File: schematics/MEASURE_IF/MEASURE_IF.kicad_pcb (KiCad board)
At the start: 2 copper layers, 45.7 x 65.2 mm, 50 parts, among them J1 SWD_CONN, J2 ARGUS_SPI_LEGACY_CONN, J3 ARGUS_SPI_FFC_CONN, J4 VMOT_IN_5mm, J5 MOT_TERM, J6 MOT_TERM, J7 USB_B_Micro, J8 MOT_TERM, J9 MOT_TERM, SW1 SW_RESET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

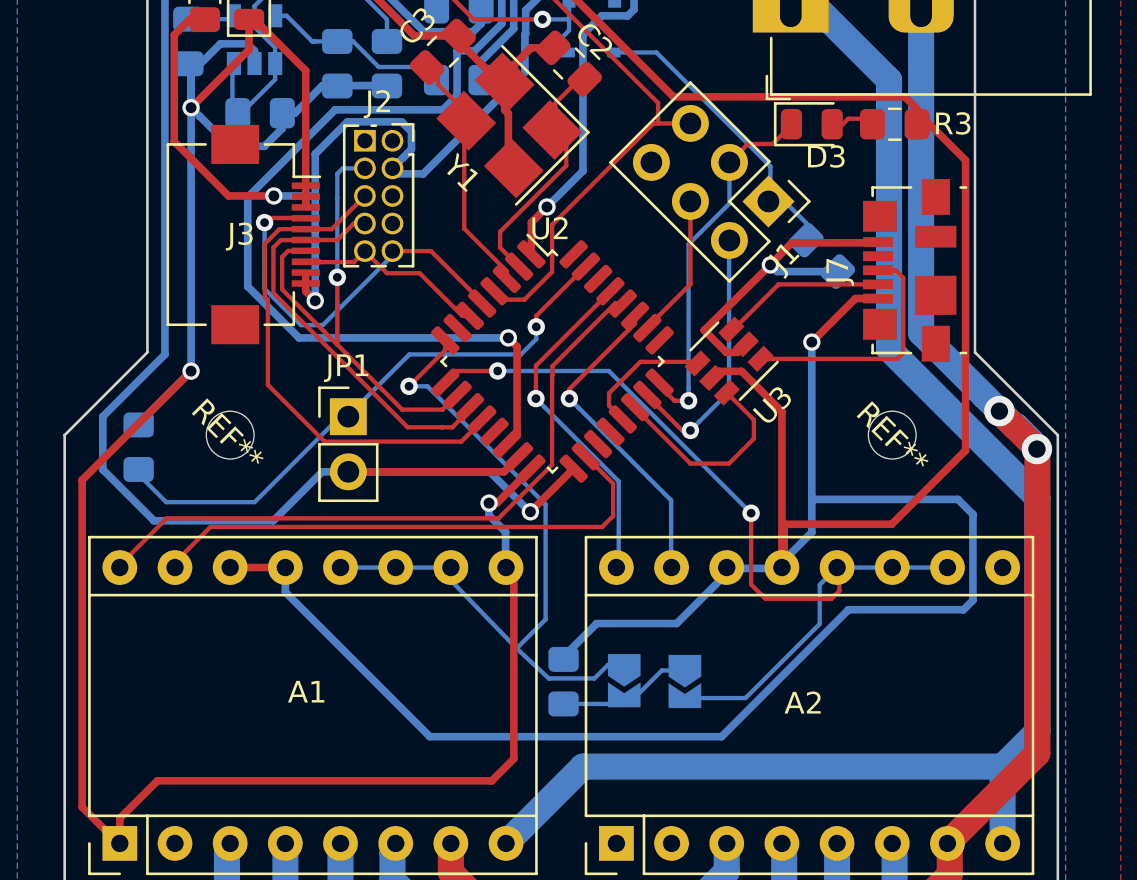
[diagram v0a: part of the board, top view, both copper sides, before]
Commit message: Fix pin location error
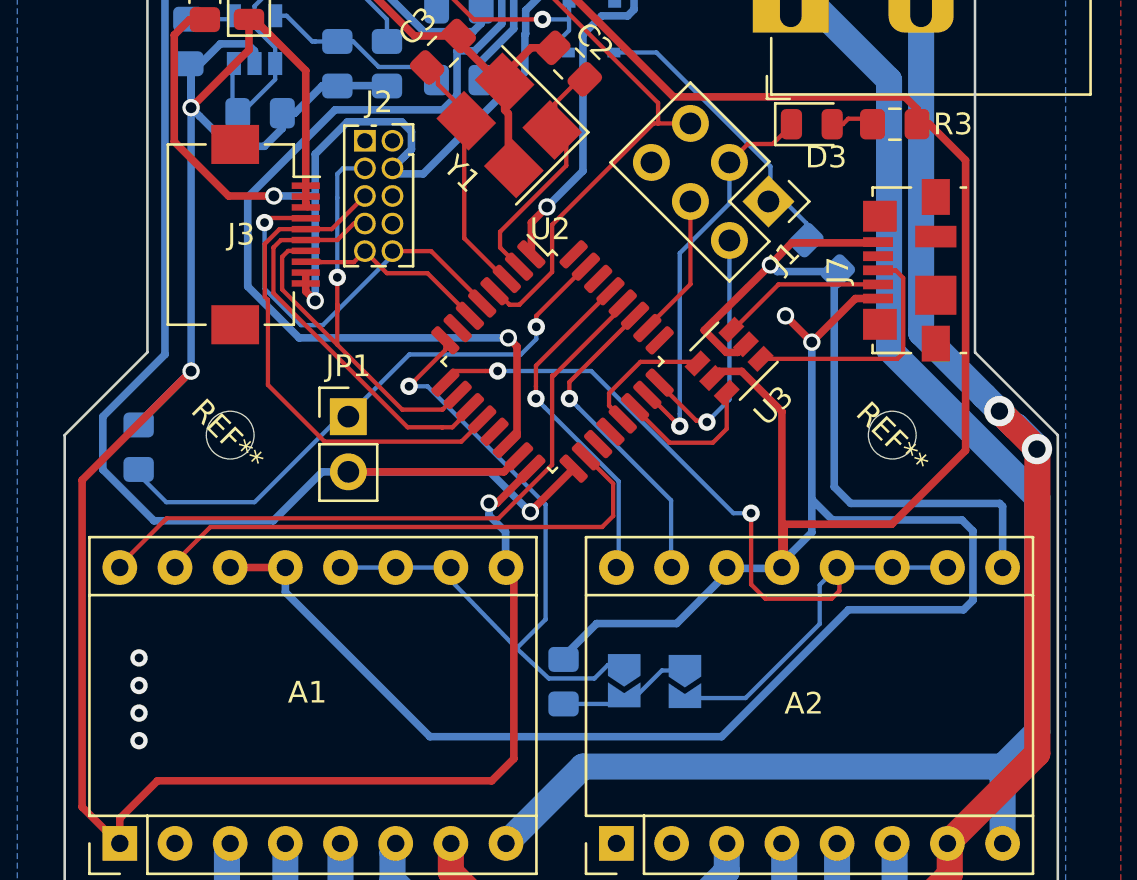
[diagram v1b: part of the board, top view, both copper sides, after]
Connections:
- U2 pad 23: /SWCLK -> /SWDIO
- U2 pad 24: /SWDIO -> /SWCLK
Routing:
- net GND: track 162.8 -> 183.4 mm, vias 6 -> 10
- net /USB_DP: track 9.09 -> 6.26 mm
- net /SWDIO: track 16.8 -> 18.3 mm
- net VCC: track 185.6 -> 186.8 mm, vias 4 -> 5
- net /SWCLK: track 12.2 -> 11.4 mm

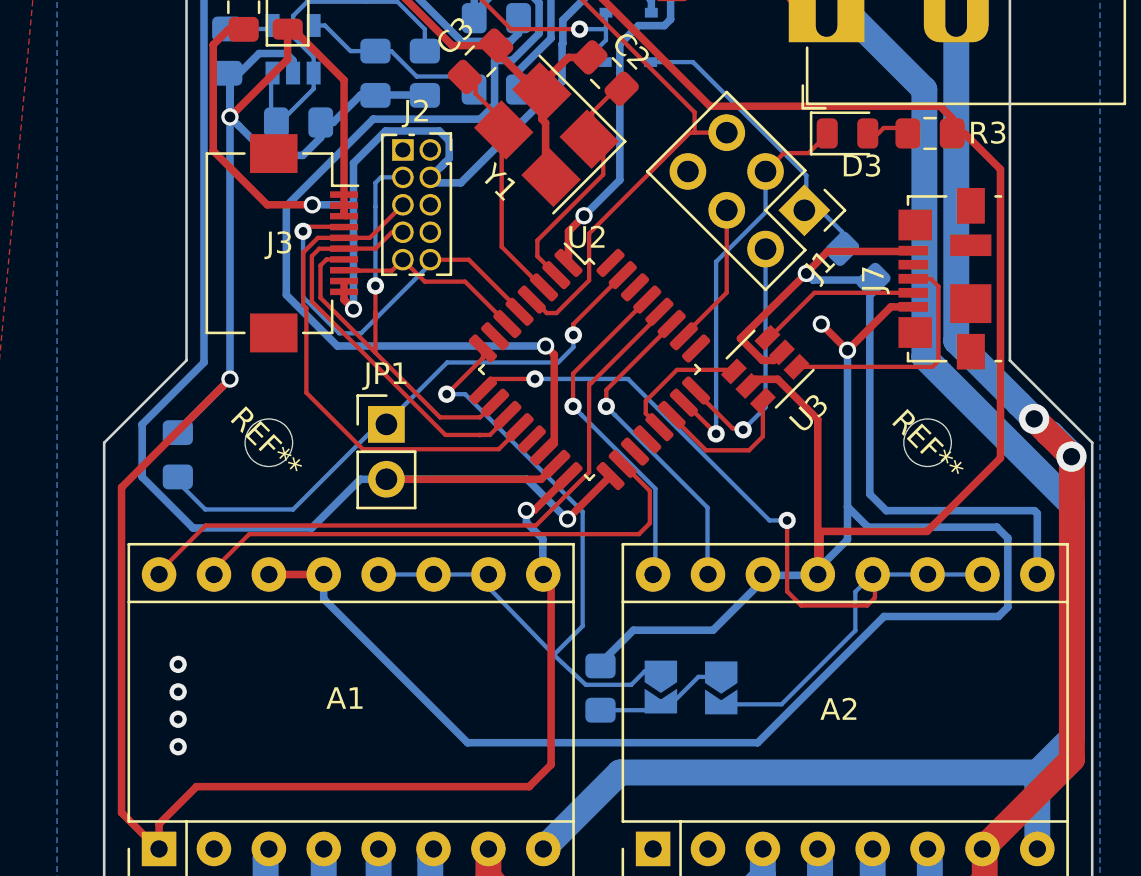
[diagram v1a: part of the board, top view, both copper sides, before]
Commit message: Connect NRST signal to motor driver
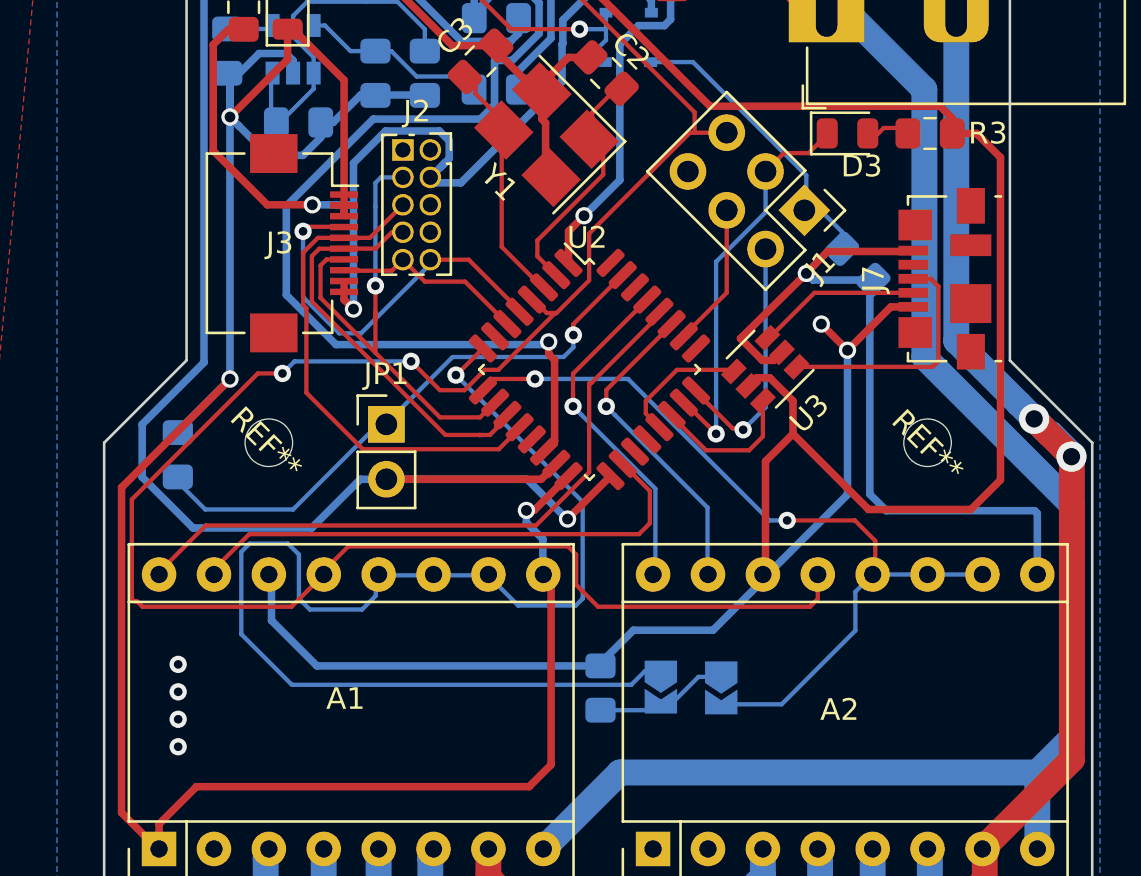
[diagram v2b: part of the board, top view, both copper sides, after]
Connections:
- A1 pad 13: VCC -> /NRST
- A2 pad 13: VCC -> /NRST
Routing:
- net /NRST: track 28.7 -> 93.9 mm, vias 1 -> 3
- net VCC: track 186.8 -> 153.1 mm
- net /MOTuCONF1: track 34.3 -> 59.4 mm
- net /MOTuCONF2: track 41.8 -> 38.9 mm

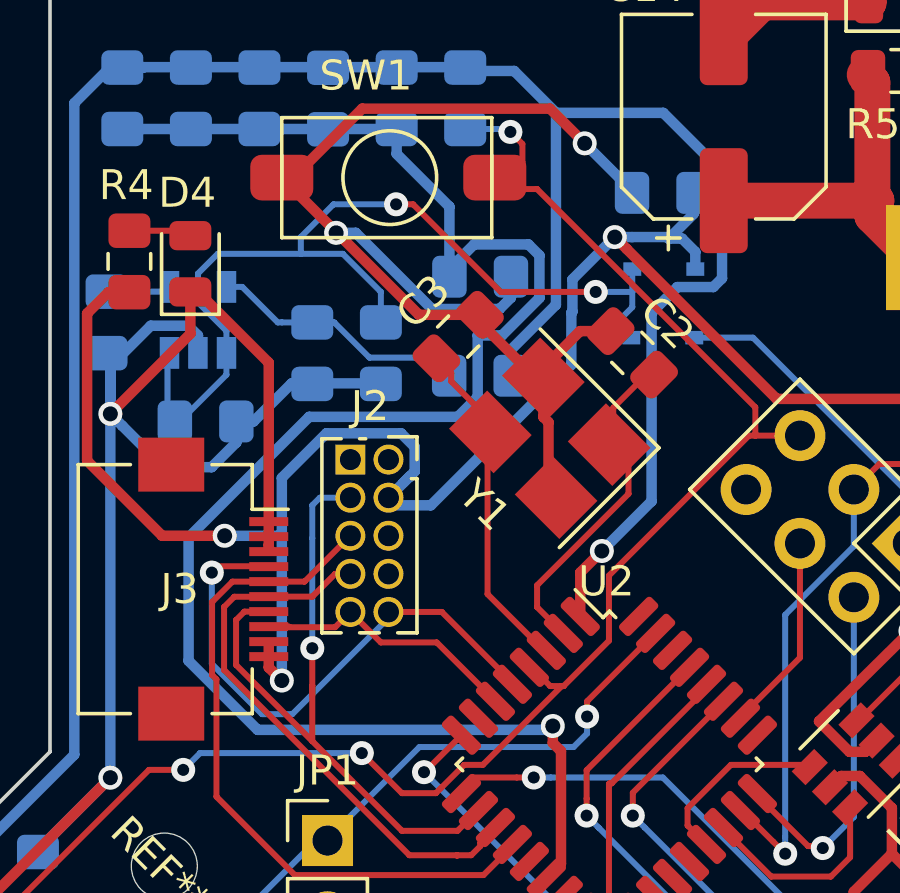
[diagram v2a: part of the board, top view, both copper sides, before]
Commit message: Fix invalid connector boundary
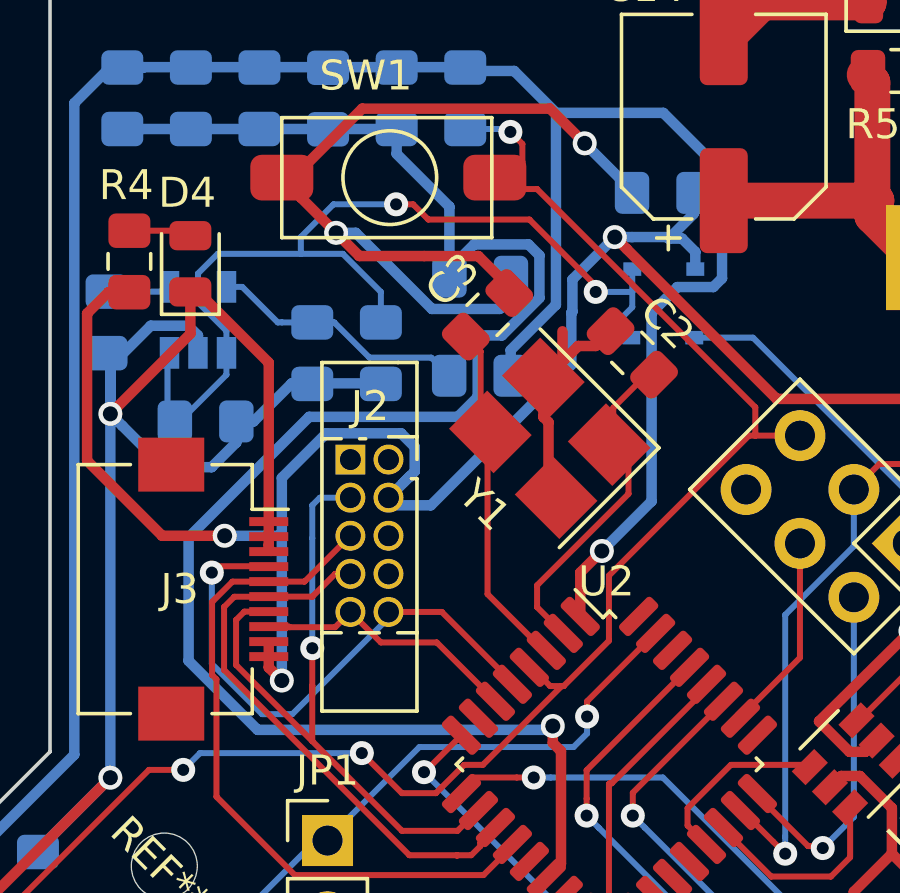
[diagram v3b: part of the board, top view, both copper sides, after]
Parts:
- moved C3 1.22 mm to (39.6, 133.6)
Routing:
- net GND: track 183.4 -> 182.6 mm
